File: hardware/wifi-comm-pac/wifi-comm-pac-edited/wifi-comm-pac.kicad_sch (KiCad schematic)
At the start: 76 parts, among them J1 Conn_02x05 IDC (P1 MODEM), J2 CMS-151103-088SP, J3 USB-C sink, J4 2x13 header, GPIO breakout (D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, J5 5V out to keyboard adapter, SW1 Slide switch, latching, U1 74LVC4T245 (TXD/MCB), U10 AP2112K-3.3 LDO, U11 TPS2553 current limit ~0.95A, U2 74LVC4T245 (CTS/RI), U3 74LVC1G07 (MSB), U4 MAX3232 (RXD), U5 ESP32-S2-MINI-2U, U6 AW9523B panel 0x58, U7 AW9523B interface 0x59, U8 MAX98357A, U9 TPS54331 buck 12.6->5

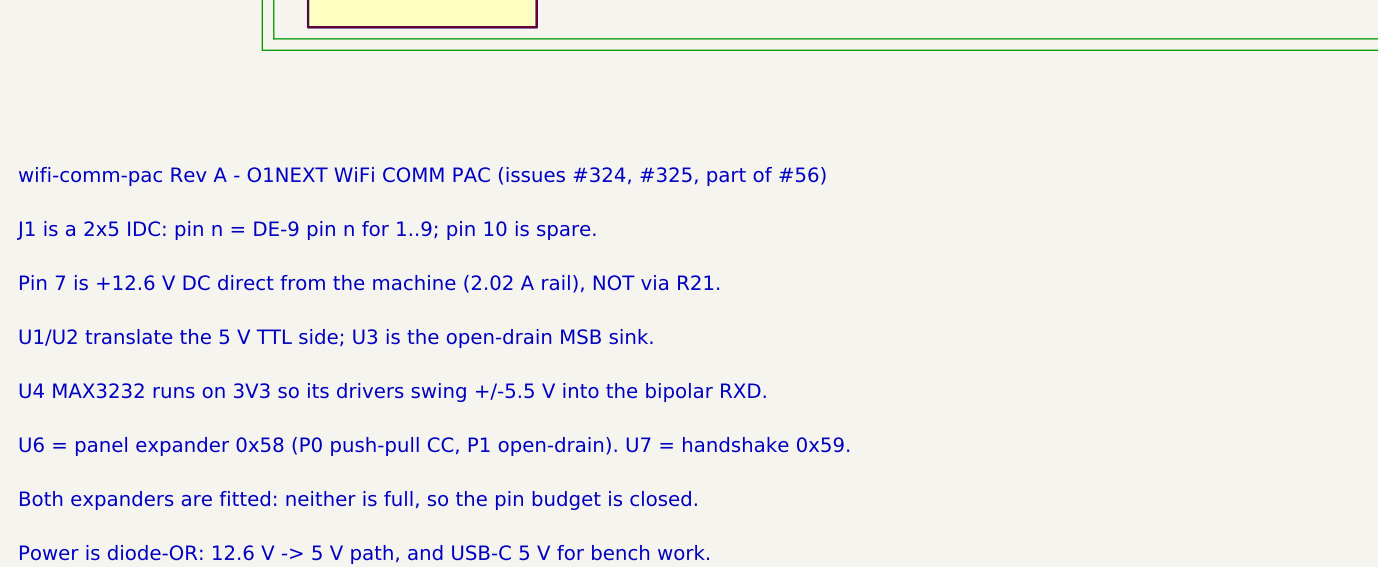
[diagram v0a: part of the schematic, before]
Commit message: the remaining READMEs: the same pass, applied outside docs/ (#353) (#355)
* docs: lead the tools index with the tree, not its history (#353)

* docs: fold the research-tool history into its findings (#353)

* docs: state the zoom and pen rules without the confession (#353)

* docs: say how to run the machine before how it got here (#353)

* docs: separate our history from picoem upstream state (#353)

* docs: run instructions before the why-not-Python argument (#353)

* docs: the register states the hardware state, and the modem finding (#353)

* hardware: pin 7 is behind the 22 ohms, and lead with the board state (#353)

* docs: eight design questions, and the relay is not a fallback (#353)

* docs: drop the dated heading and the superseded board list (#353)

* docs: lead Rev A with what it is and where it stands (#353)

* docs: no schematic yet, and #48 on the item it settles (#353)

* docs: the front door says what o1next is, before the boards (#353)

* firmware: the radio is off the bus-critical chip, and where the tree stands (#353)

* firmware: bench-bridge to what a reader needs (#353)

* firmware: three switches remain, and the retirement is the reason (#353)

* firmware: screenpac-video leads with its state (#353)

* site: the wordmark moved, and the pipeline stands as written (#353)

* hardware: P5 is not current limited, so the budget is the PSU 2.02 A (#354)

* hardware: the schematic note says pin 7 is behind R21 (#56)

* hardware: correct the pin-7 note in the generated schematic (#56)

* hardware: correct the pin-7 note in the edited schematic (#56)

* hardware: the rail monitor argument, restated for a limited pin 7 (#56)

* tools: three SDK switches remain, not six (#353)

* docs: wrap the front-door paragraph to match the docs branch (#353)

* hardware: one final Power text, shared with the docs branch (#353, #56)

* hardware: the +12 V rail has room to spare (#354)
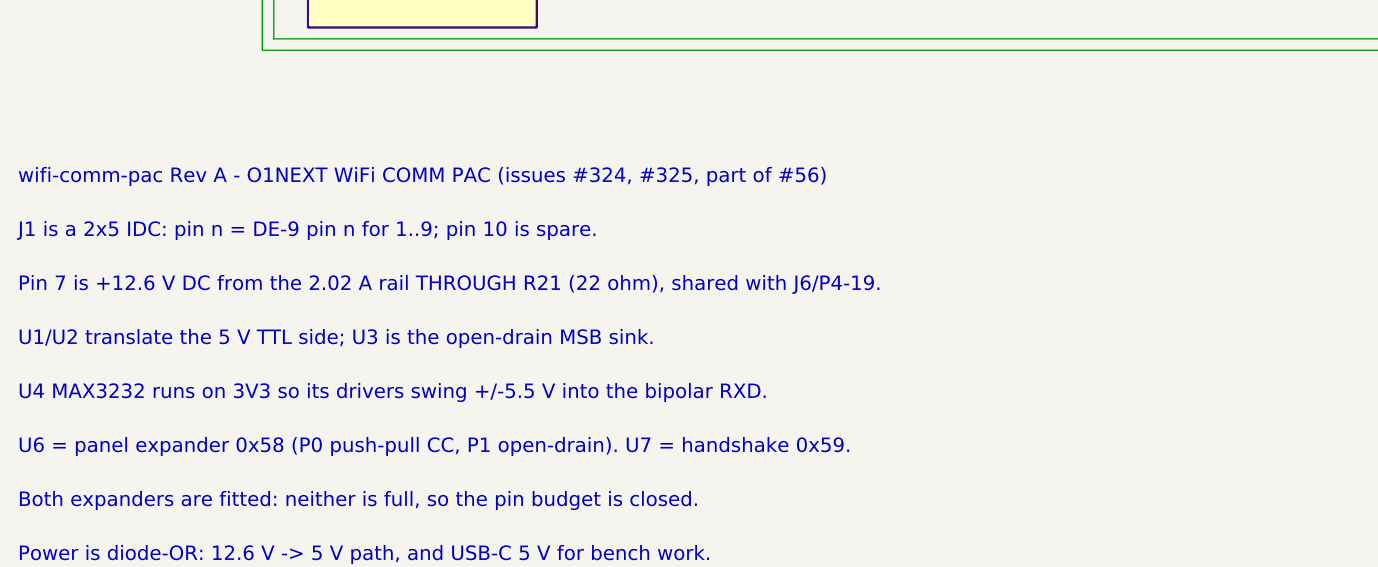
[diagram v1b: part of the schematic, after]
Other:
- note added: "Pin 7 is +12.6 V DC from the 2.02 A rail THROUGH R21 (22 ohm), shared with J6/P4-19."
- note removed: "Pin 7 is +12.6 V DC direct from the machine (2.02 A rail), NOT via R21."
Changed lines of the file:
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@@
   (text "wifi-comm-pac Rev A - O1NEXT WiFi COMM PAC (issues #324, #325, part of #56)" (at 30 545 0) (effects (font (size 1.6 1.6)) (justify left)))
   (text "J1 is a 2x5 IDC: pin n = DE-9 pin n for 1..9; pin 10 is spare." (at 30 551 0) (effects (font (size 1.6 1.6)) (justify left)))
-  (text "Pin 7 is +12.6 V DC direct from the machine (2.02 A rail), NOT via R21." (at 30 557 0) (effects (font (size 1.6 1.6)) (justify left)))
+  (text "Pin 7 is +12.6 V DC from the 2.02 A rail THROUGH R21 (22 ohm), shared with J6/P4-19." (at 30 557 0) (effects (font (size 1.6 1.6)) (justify left)))
   (text "U1/U2 translate the 5 V TTL side; U3 is the open-drain MSB sink." (at 30 563 0) (effects (font (size 1.6 1.6)) (justify left)))
   (text "U4 MAX3232 runs on 3V3 so its drivers swing +/-5.5 V into the bipolar RXD." (at 30 569 0) (effects (font (size 1.6 1.6)) (justify left)))
